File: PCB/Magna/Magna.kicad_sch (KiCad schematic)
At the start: 1 part, among them J101 Conn_02x08_Counter_Clockwise

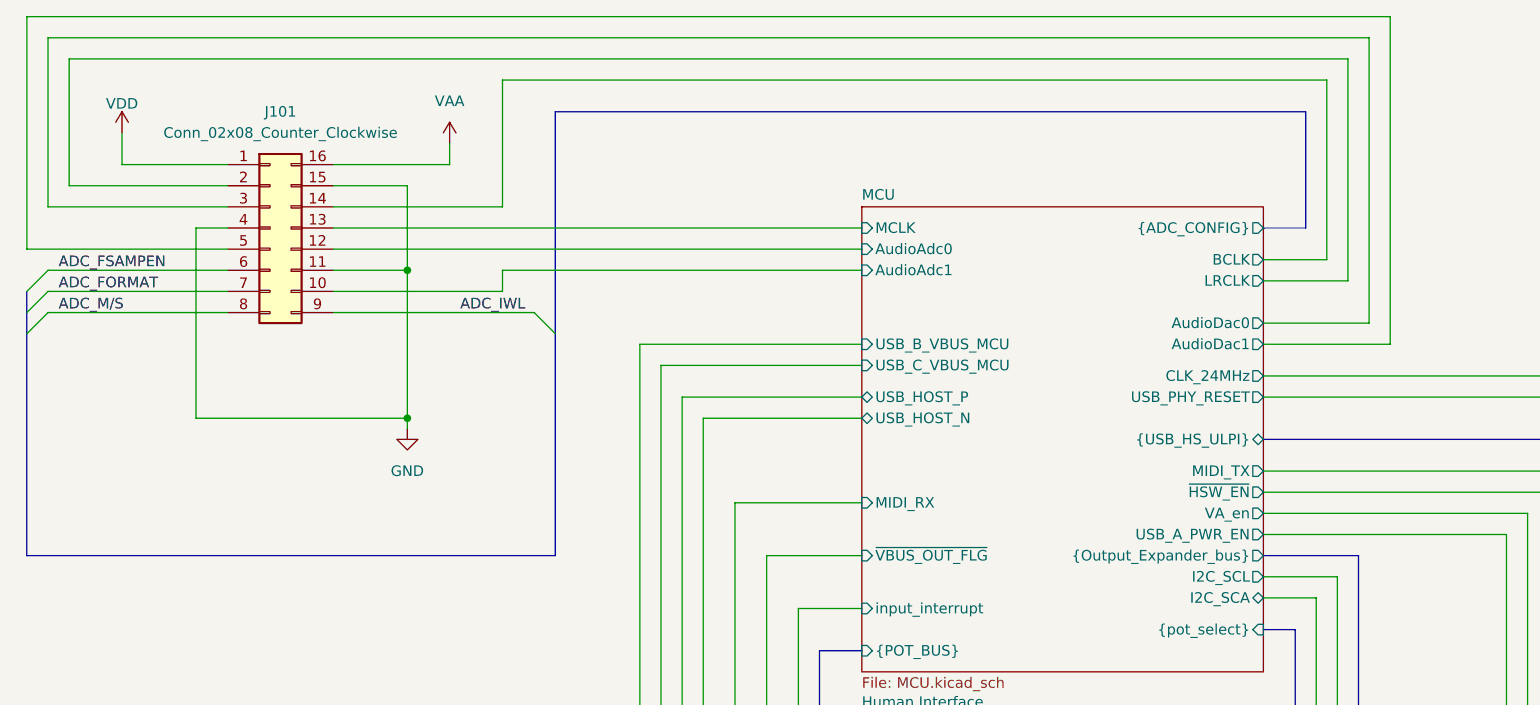
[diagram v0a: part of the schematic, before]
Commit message: Update Audio connector pinning (#14)
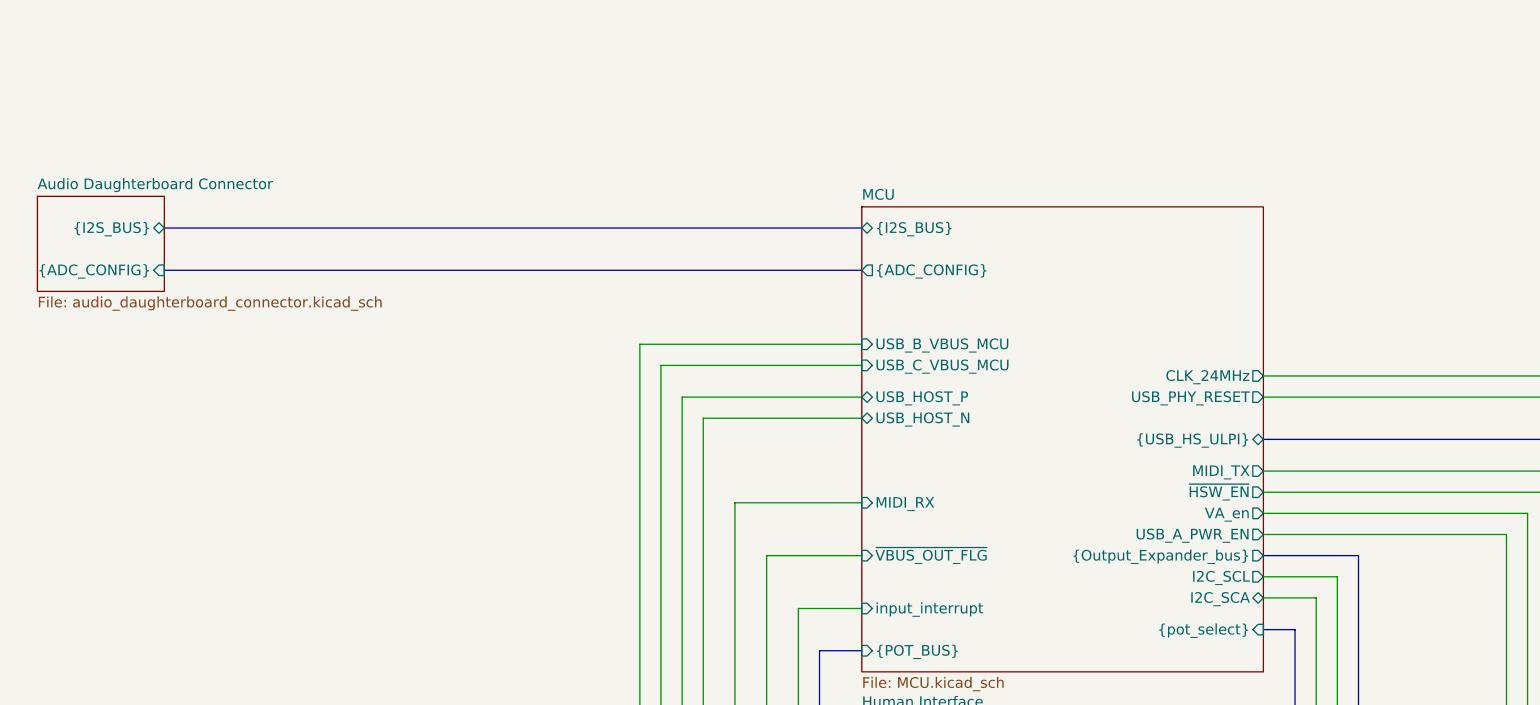
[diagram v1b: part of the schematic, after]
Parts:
- removed J101: Conn_02x08_Counter_Clockwise, Connector_PinSocket_2.54mm:PinSocket_2x08_P2.54mm_Vertical, symbol Connector_Generic:Conn_02x08_Counter_Clockwise
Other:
- added sheet Audio Daughterboard Connector (audio_daughterboard_connector.kicad_sch)
- sheet MCU ports: added {I2S_BUS}; removed AudioAdc0, AudioAdc1, AudioDac0, AudioDac1, BCLK, LRCLK, MCLK

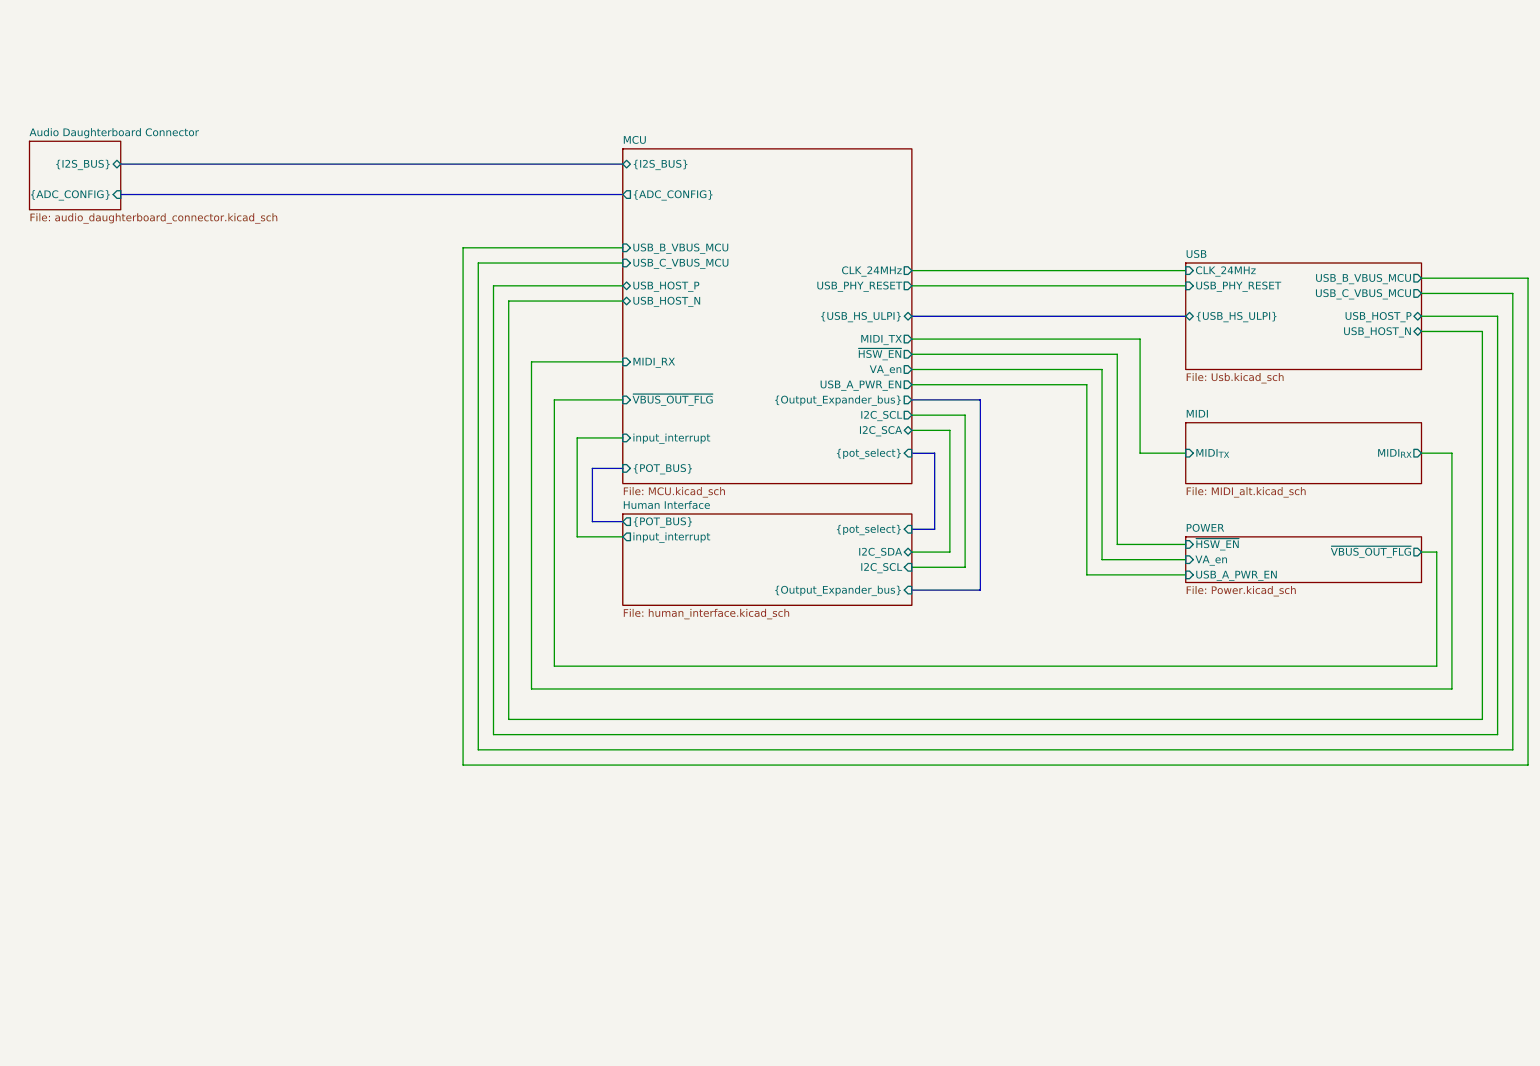
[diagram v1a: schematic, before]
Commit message: Update connector on ADC board and clean up MCU sheet
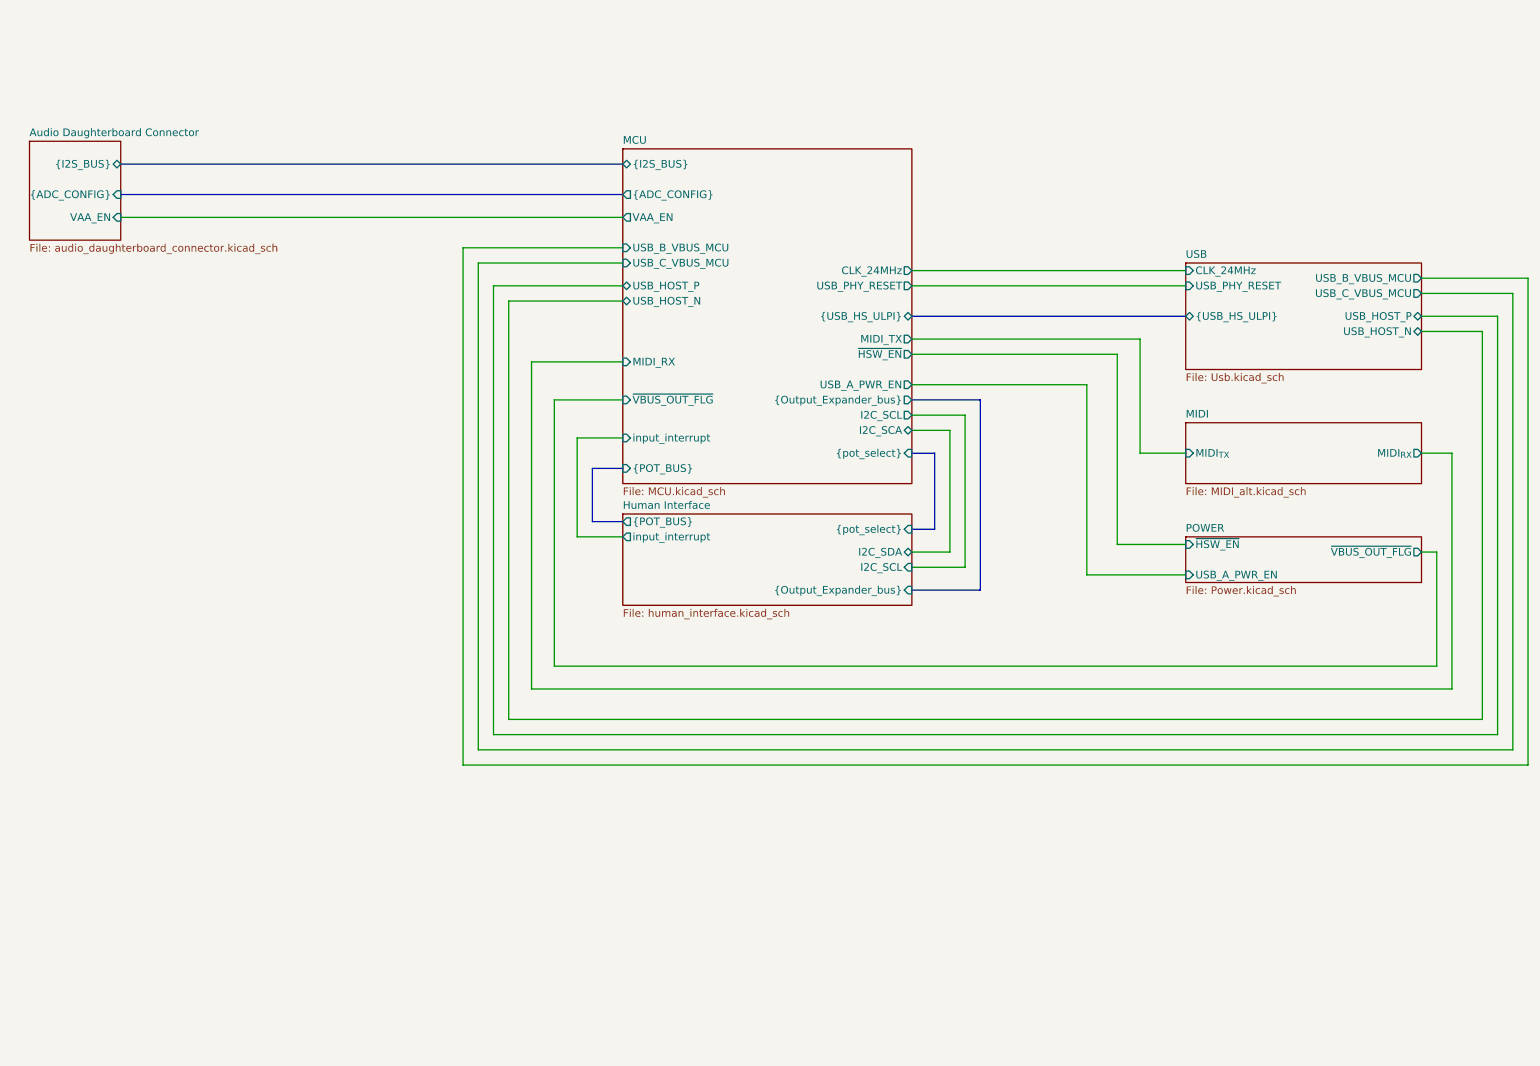
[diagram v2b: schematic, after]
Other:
- sheet Audio Daughterboard Connector ports: added VAA_EN; removed none
- sheet MCU ports: added VAA_EN; removed VA_en
- sheet POWER ports: added none; removed VA_en
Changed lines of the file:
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@@
-    (stroke (width 0) (type default))
-  )
-  (wire (pts (xy 173.99 82.55) (xy 205.74 82.55))
     (stroke (width 0) (type default))
   )
@@
     (stroke (width 0) (type default))
   )
-  (wire (pts (xy 205.74 82.55) (xy 205.74 114.3))
-    (stroke (width 0) (type default))
-  )
   (bus (pts (xy 125.73 107.95) (xy 120.65 107.95))
     (stroke (width 0) (type default))
@@
     (stroke (width 0) (type default))
   )
-  (wire (pts (xy 205.74 114.3) (xy 219.71 114.3))
+  (wire (pts (xy 41.91 57.15) (xy 125.73 57.15))
     (stroke (width 0) (type default))
   )
@@
       (effects (font (size 1.27 1.27)) (justify right))
     )
-    (pin "VA_en" output (at 173.99 82.55 0)
-      (effects (font (size 1.27 1.27)) (justify right))
+    (pin "VAA_EN" output (at 125.73 57.15 180)
+      (effects (font (size 1.27 1.27)) (justify left))
     )
     (pin "USB_A_PWR_EN" output (at 173.99 85.09 0)
@@
       (effects (font (size 1.27 1.27)) (justify left top))
     )
-    (pin "VA_en" input (at 219.71 114.3 180)
-      (effects (font (size 1.27 1.27)) (justify left))
-    )
     (pin "~{HSW_EN}" input (at 219.71 111.76 180)
       (effects (font (size 1.27 1.27)) (justify left))
@@
     )
   )
-  (sheet (at 26.67 44.45) (size 15.24 11.43) (fields_autoplaced)
+  (sheet (at 26.67 44.45) (size 15.24 16.51) (fields_autoplaced)
     (stroke (width 0.1524) (type solid))
     (fill (color 0 0 0 0.0000))
@@
       (effects (font (size 1.27 1.27)) (justify left bottom))
     )
-    (property "Sheetfile" "audio_daughterboard_connector.kicad_sch" (at 26.67 56.4646 0)
+    (property "Sheetfile" "audio_daughterboard_connector.kicad_sch" (at 26.67 61.5446 0)
       (effects (font (size 1.27 1.27)) (justify left top))
     )
@@
       (effects (font (size 1.27 1.27)) (justify right))
     )
+    (pin "VAA_EN" input (at 41.91 57.15 0)
+      (effects (font (size 1.27 1.27)) (justify right))
+    )

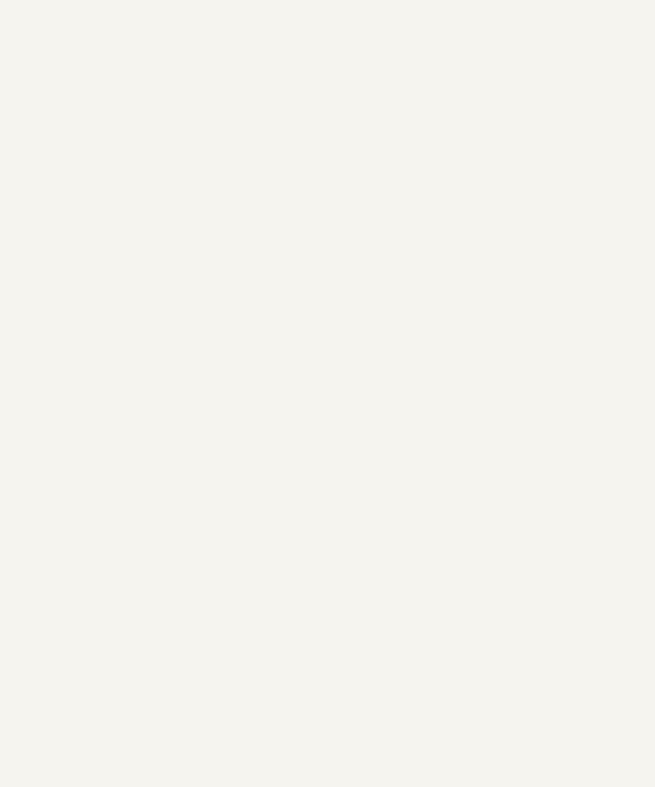
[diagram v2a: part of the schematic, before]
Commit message: Mainboard layout (#19)
Also adds mounting holes to IO daughterboard
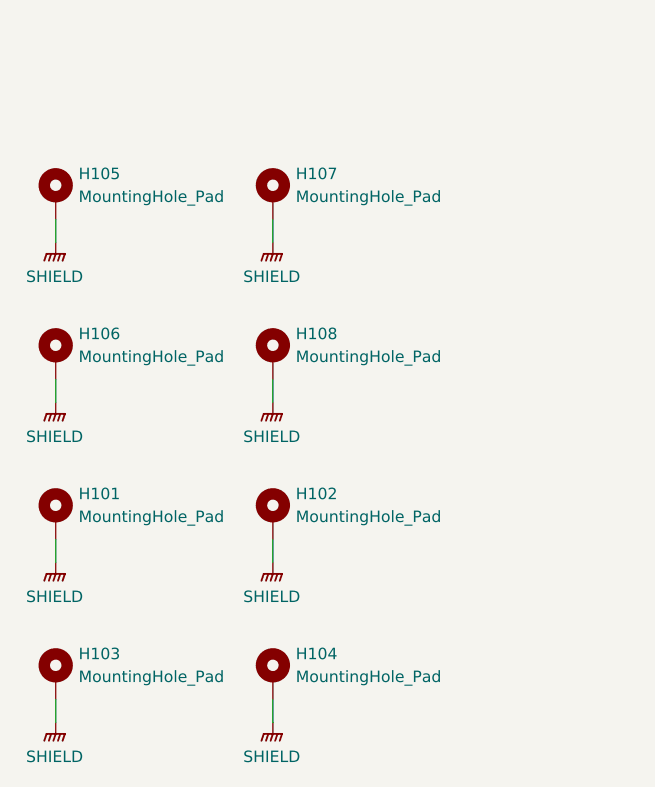
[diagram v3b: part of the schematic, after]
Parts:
- added H101, H102, H103, H104, H105, H106, H107, H108: MountingHole_Pad, MountingHole:MountingHole_3.2mm_M3_Pad_Via, symbol Mechanical:MountingHole_Pad
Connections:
- new net SHIELD: H101.1, H102.1, H103.1, H104.1, H105.1, H106.1, H107.1, H108.1

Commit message: Update some files to KiCad8 and make ready for production
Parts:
- H101, H102, H103, H104, H105, H106, H107, H108: now left out of the parts list
